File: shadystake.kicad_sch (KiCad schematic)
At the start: 15 parts, among them J1 6P6C, J2 6P6C, J3 6P6C, J4 6P6C, J5 6P6C, J6 6P6C, J7 8P8C

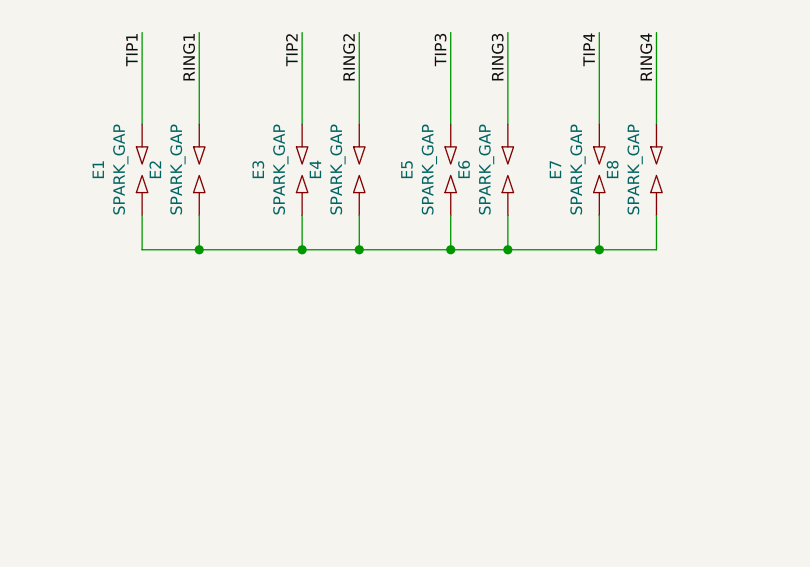
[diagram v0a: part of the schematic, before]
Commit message: really rough draft of physical layout
⚠ spark gap footprints still completely missing

modular jack footprints assumed to be the Amphenol SKU.

The Board.Cuts shape still seems like awkward proportions, but in a
manufacturable size.
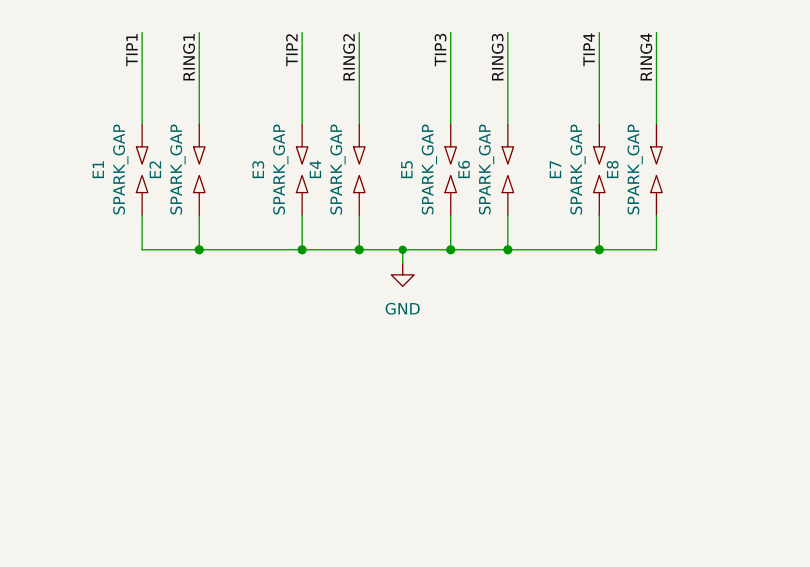
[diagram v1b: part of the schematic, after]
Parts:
- J1, J2, J3, J4, J5, J6: footprint Connect:RJ12_E -> Connector_RJ:RJ12_Amphenol_54601
- J7: footprint Connect:RJ45_8 -> Connector_RJ:RJ45_Amphenol_54602-x08_Horizontal
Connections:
- net GND: now reaches E1.1, E2.1, E3.1, E4.1, E5.1, E6.1, E7.1, E8.1

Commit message: shadystake: make it roughly the proportions of the Shadytel logo
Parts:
- E1, E2, E3, E4, E5, E6, E7, E8: footprint (none) -> Shadystake:Sparkgap_JLC
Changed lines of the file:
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@@
     (property "Reference" "E1" (id 0) (at 133.604 91.44 0))
     (property "Value" "SPARK_GAP" (id 1) (at 135.9154 91.44 0))
-    (property "Footprint" "" (id 2) (at 140.208 91.44 0)
+    (property "Footprint" "Shadystake:Sparkgap_JLC" (id 2) (at 140.208 91.44 0)
       (effects (font (size 1.27 1.27)) hide)
     )
@@
     (property "Reference" "E2" (id 0) (at 139.954 91.44 0))
     (property "Value" "SPARK_GAP" (id 1) (at 142.2654 91.44 0))
-    (property "Footprint" "" (id 2) (at 146.558 91.44 0)
+    (property "Footprint" "Shadystake:Sparkgap_JLC" (id 2) (at 146.558 91.44 0)
       (effects (font (size 1.27 1.27)) hide)
     )
@@
     (property "Reference" "E4" (id 0) (at 157.734 91.44 0))
     (property "Value" "SPARK_GAP" (id 1) (at 160.0454 91.44 0))
-    (property "Footprint" "" (id 2) (at 164.338 91.44 0)
+    (property "Footprint" "Shadystake:Sparkgap_JLC" (id 2) (at 164.338 91.44 0)
       (effects (font (size 1.27 1.27)) hide)
     )
@@
     (property "Reference" "E3" (id 0) (at 151.384 91.44 0))
     (property "Value" "SPARK_GAP" (id 1) (at 153.6954 91.44 0))
-    (property "Footprint" "" (id 2) (at 157.988 91.44 0)
+    (property "Footprint" "Shadystake:Sparkgap_JLC" (id 2) (at 157.988 91.44 0)
       (effects (font (size 1.27 1.27)) hide)
     )
@@
     (property "Reference" "E5" (id 0) (at 167.894 91.44 0))
     (property "Value" "SPARK_GAP" (id 1) (at 170.2054 91.44 0))
-    (property "Footprint" "" (id 2) (at 174.498 91.44 0)
+    (property "Footprint" "Shadystake:Sparkgap_JLC" (id 2) (at 174.498 91.44 0)
       (effects (font (size 1.27 1.27)) hide)
     )
@@
     (property "Reference" "E6" (id 0) (at 174.244 91.44 0))
     (property "Value" "SPARK_GAP" (id 1) (at 176.5554 91.44 0))
-    (property "Footprint" "" (id 2) (at 180.848 91.44 0)
+    (property "Footprint" "Shadystake:Sparkgap_JLC" (id 2) (at 180.848 91.44 0)
       (effects (font (size 1.27 1.27)) hide)
     )
@@
     (property "Reference" "E7" (id 0) (at 184.404 91.44 0))
     (property "Value" "SPARK_GAP" (id 1) (at 186.7154 91.44 0))
-    (property "Footprint" "" (id 2) (at 191.008 91.44 0)
+    (property "Footprint" "Shadystake:Sparkgap_JLC" (id 2) (at 191.008 91.44 0)
       (effects (font (size 1.27 1.27)) hide)
     )
@@
     (property "Reference" "E8" (id 0) (at 190.754 91.44 0))
     (property "Value" "SPARK_GAP" (id 1) (at 193.0654 91.44 0))
-    (property "Footprint" "" (id 2) (at 197.358 91.44 0)
+    (property "Footprint" "Shadystake:Sparkgap_JLC" (id 2) (at 197.358 91.44 0)
       (effects (font (size 1.27 1.27)) hide)
     )
@@
     )
     (path "/00000000-0000-0000-0000-00005e77f6d5"
-      (reference "E1") (unit 1) (value "SPARK_GAP") (footprint "")
+      (reference "E1") (unit 1) (value "SPARK_GAP") (footprint "Shadystake:Sparkgap_JLC")
     )
     (path "/00000000-0000-0000-0000-00005e77fd1f"
-      (reference "E2") (unit 1) (value "SPARK_GAP") (footprint "")
+      (reference "E2") (unit 1) (value "SPARK_GAP") (footprint "Shadystake:Sparkgap_JLC")
     )
     (path "/00000000-0000-0000-0000-00005e7804e5"
-      (reference "E3") (unit 1) (value "SPARK_GAP") (footprint "")
+      (reference "E3") (unit 1) (value "SPARK_GAP") (footprint "Shadystake:Sparkgap_JLC")
     )
     (path "/00000000-0000-0000-0000-00005e77fe7e"
-      (reference "E4") (unit 1) (value "SPARK_GAP") (footprint "")
+      (reference "E4") (unit 1) (value "SPARK_GAP") (footprint "Shadystake:Sparkgap_JLC")
     )
     (path "/00000000-0000-0000-0000-00005e780786"
-      (reference "E5") (unit 1) (value "SPARK_GAP") (footprint "")
+      (reference "E5") (unit 1) (value "SPARK_GAP") (footprint "Shadystake:Sparkgap_JLC")
     )
     (path "/00000000-0000-0000-0000-00005e780e1b"
-      (reference "E6") (unit 1) (value "SPARK_GAP") (footprint "")
+      (reference "E6") (unit 1) (value "SPARK_GAP") (footprint "Shadystake:Sparkgap_JLC")
     )
     (path "/00000000-0000-0000-0000-00005e7810bc"
-      (reference "E7") (unit 1) (value "SPARK_GAP") (footprint "")
+      (reference "E7") (unit 1) (value "SPARK_GAP") (footprint "Shadystake:Sparkgap_JLC")
     )
     (path "/00000000-0000-0000-0000-00005e781e02"
-      (reference "E8") (unit 1) (value "SPARK_GAP") (footprint "")
+      (reference "E8") (unit 1) (value "SPARK_GAP") (footprint "Shadystake:Sparkgap_JLC")
     )
     (path "/00000000-0000-0000-0000-00005e77093f"

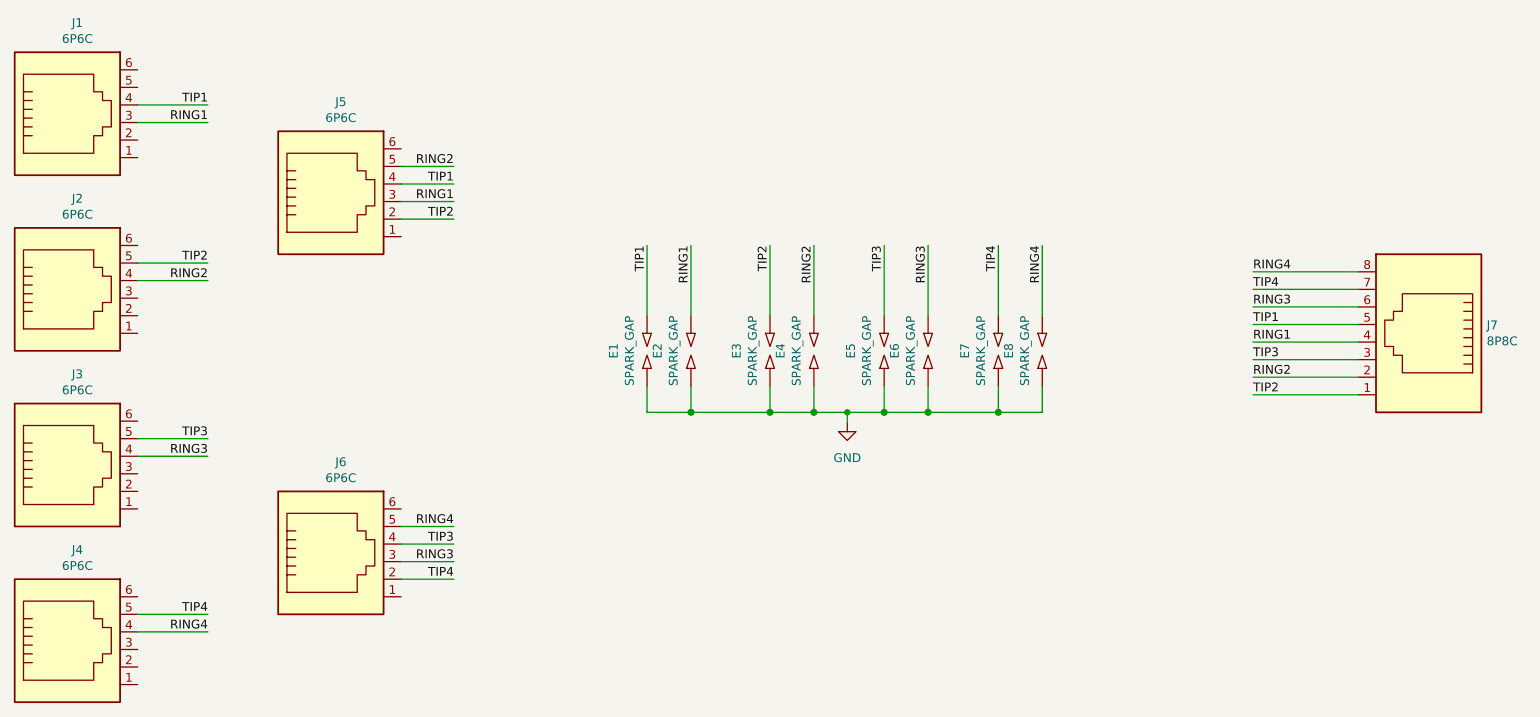
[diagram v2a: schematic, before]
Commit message: Fix pin connections on several jacks and add more spark gaps
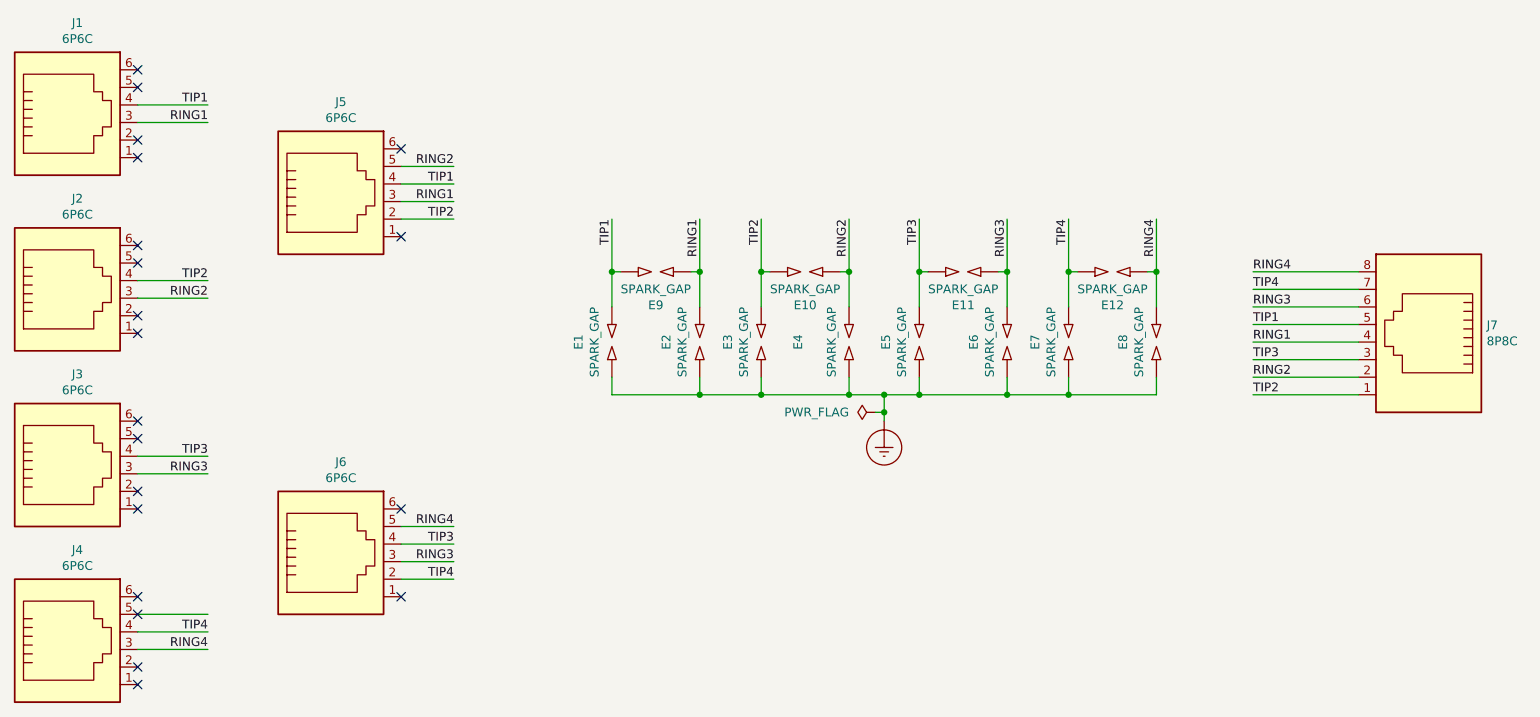
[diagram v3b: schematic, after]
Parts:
- added E10, E11, E12, E9: SPARK_GAP, shadytel:SPARKGAP, symbol shadystake-rescue:SPARK_GAP-Device
- E1, E2, E3, E4, E5, E6, E7, E8: footprint Shadystake:Sparkgap_JLC -> shadytel:SPARKGAP
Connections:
- net RING1: now also E9.1
- net RING2: now also J2.3, E10.1; no longer J2.4
- net RING3: now also J3.3, E11.1; no longer J3.4
- net RING4: now also J4.3, E12.1; no longer J4.4
- net TIP1: now also E9.2
- net TIP2: now also J2.4, E10.2; no longer J2.5
- net TIP3: now also J3.4, E11.2; no longer J3.5
- net TIP4: now also J4.4, E12.2; no longer J4.5
- net GND renamed Earth_Protective
- no-connect marks 0 -> 20
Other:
- moved on the sheet: E1, E2, E3, E4, E5, E6, E7, E8

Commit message: fix spark gaps, continuity on PCB
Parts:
- E1, E10, E11, E12, E2, E3, E4, E5, E6, E7, E8, E9: footprint shadytel:SPARKGAP -> Shadystake:Sparkgap_JLC
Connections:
- net RING2: now also E10.2; no longer E10.1
- net RING3: now also E11.2; no longer E11.1
- net TIP2: now also E10.1; no longer E10.2
- net TIP3: now also E11.1; no longer E11.2
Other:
- moved on the sheet: E10, E11
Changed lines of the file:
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@@
     (property "Reference" "E1" (id 0) (at 128.524 90.17 0))
     (property "Value" "SPARK_GAP" (id 1) (at 130.8354 90.17 0))
-    (property "Footprint" "shadytel:SPARKGAP" (id 2) (at 135.128 90.17 0)
+    (property "Footprint" "Shadystake:Sparkgap_JLC" (id 2) (at 135.128 90.17 0)
       (effects (font (size 1.27 1.27)) hide)
     )
@@
     (property "Reference" "E2" (id 0) (at 141.224 90.17 0))
     (property "Value" "SPARK_GAP" (id 1) (at 143.5354 90.17 0))
-    (property "Footprint" "shadytel:SPARKGAP" (id 2) (at 147.828 90.17 0)
+    (property "Footprint" "Shadystake:Sparkgap_JLC" (id 2) (at 147.828 90.17 0)
       (effects (font (size 1.27 1.27)) hide)
     )
@@
     (property "Reference" "E4" (id 0) (at 160.274 90.17 0))
     (property "Value" "SPARK_GAP" (id 1) (at 165.1254 90.17 0))
-    (property "Footprint" "shadytel:SPARKGAP" (id 2) (at 169.418 90.17 0)
+    (property "Footprint" "Shadystake:Sparkgap_JLC" (id 2) (at 169.418 90.17 0)
       (effects (font (size 1.27 1.27)) hide)
     )
@@
     (property "Reference" "E3" (id 0) (at 150.114 90.17 0))
     (property "Value" "SPARK_GAP" (id 1) (at 152.4254 90.17 0))
-    (property "Footprint" "shadytel:SPARKGAP" (id 2) (at 156.718 90.17 0)
+    (property "Footprint" "Shadystake:Sparkgap_JLC" (id 2) (at 156.718 90.17 0)
       (effects (font (size 1.27 1.27)) hide)
     )
@@
     (property "Reference" "E5" (id 0) (at 172.974 90.17 0))
     (property "Value" "SPARK_GAP" (id 1) (at 175.2854 90.17 0))
-    (property "Footprint" "shadytel:SPARKGAP" (id 2) (at 179.578 90.17 0)
+    (property "Footprint" "Shadystake:Sparkgap_JLC" (id 2) (at 179.578 90.17 0)
       (effects (font (size 1.27 1.27)) hide)
     )
@@
     (property "Reference" "E6" (id 0) (at 185.674 90.17 0))
     (property "Value" "SPARK_GAP" (id 1) (at 187.9854 90.17 0))
-    (property "Footprint" "shadytel:SPARKGAP" (id 2) (at 192.278 90.17 0)
+    (property "Footprint" "Shadystake:Sparkgap_JLC" (id 2) (at 192.278 90.17 0)
       (effects (font (size 1.27 1.27)) hide)
     )
@@
     (property "Reference" "E7" (id 0) (at 194.564 90.17 0))
     (property "Value" "SPARK_GAP" (id 1) (at 196.8754 90.17 0))
-    (property "Footprint" "shadytel:SPARKGAP" (id 2) (at 201.168 90.17 0)
+    (property "Footprint" "Shadystake:Sparkgap_JLC" (id 2) (at 201.168 90.17 0)
       (effects (font (size 1.27 1.27)) hide)
     )
@@
     (property "Reference" "E8" (id 0) (at 207.264 90.17 0))
     (property "Value" "SPARK_GAP" (id 1) (at 209.5754 90.17 0))
-    (property "Footprint" "shadytel:SPARKGAP" (id 2) (at 213.868 90.17 0)
+    (property "Footprint" "Shadystake:Sparkgap_JLC" (id 2) (at 213.868 90.17 0)
       (effects (font (size 1.27 1.27)) hide)
     )
@@
     (pin "2")
   )
-  (symbol (lib_id "shadystake-rescue:SPARK_GAP-Device") (at 161.29 80.01 180) (unit 1)
+  (symbol (lib_id "shadystake-rescue:SPARK_GAP-Device") (at 161.29 80.01 0) (mirror x) (unit 1)
     (in_bom yes) (on_board yes)
     (property "Reference" "E10" (id 0) (at 161.29 84.836 0))
     (property "Value" "SPARK_GAP" (id 1) (at 161.29 82.5246 0))
-    (property "Footprint" "shadytel:SPARKGAP" (id 2) (at 161.29 78.232 0)
+    (property "Footprint" "Shadystake:Sparkgap_JLC" (id 2) (at 161.29 78.232 0)
       (effects (font (size 1.27 1.27)) hide)
     )
@@
     (pin "2")
   )
-  (symbol (lib_id "shadystake-rescue:SPARK_GAP-Device") (at 184.15 80.01 180) (unit 1)
+  (symbol (lib_id "shadystake-rescue:SPARK_GAP-Device") (at 184.15 80.01 0) (mirror x) (unit 1)
     (in_bom yes) (on_board yes)
     (property "Reference" "E11" (id 0) (at 184.15 84.836 0))
     (property "Value" "SPARK_GAP" (id 1) (at 184.15 82.5246 0))
-    (property "Footprint" "shadytel:SPARKGAP" (id 2) (at 184.15 78.232 0)
+    (property "Footprint" "Shadystake:Sparkgap_JLC" (id 2) (at 184.15 78.232 0)
       (effects (font (size 1.27 1.27)) hide)
     )
@@
     (property "Reference" "E12" (id 0) (at 205.74 84.836 0))
     (property "Value" "SPARK_GAP" (id 1) (at 205.74 82.5246 0))
-    (property "Footprint" "shadytel:SPARKGAP" (id 2) (at 205.74 78.232 0)
+    (property "Footprint" "Shadystake:Sparkgap_JLC" (id 2) (at 205.74 78.232 0)
       (effects (font (size 1.27 1.27)) hide)
     )
@@
     (property "Reference" "E9" (id 0) (at 139.7 84.836 0))
     (property "Value" "SPARK_GAP" (id 1) (at 139.7 82.5246 0))
-    (property "Footprint" "shadytel:SPARKGAP" (id 2) (at 139.7 78.232 0)
+    (property "Footprint" "Shadystake:Sparkgap_JLC" (id 2) (at 139.7 78.232 0)
       (effects (font (size 1.27 1.27)) hide)
     )
@@
     )
     (path "/00000000-0000-0000-0000-00005e77f6d5"
-      (reference "E1") (unit 1) (value "SPARK_GAP") (footprint "shadytel:SPARKGAP")
+      (reference "E1") (unit 1) (value "SPARK_GAP") (footprint "Shadystake:Sparkgap_JLC")
     )
     (path "/00000000-0000-0000-0000-00005e77fd1f"
-      (reference "E2") (unit 1) (value "SPARK_GAP") (footprint "shadytel:SPARKGAP")
+      (reference "E2") (unit 1) (value "SPARK_GAP") (footprint "Shadystake:Sparkgap_JLC")
     )
     (path "/00000000-0000-0000-0000-00005e7804e5"
-      (reference "E3") (unit 1) (value "SPARK_GAP") (footprint "shadytel:SPARKGAP")
+      (reference "E3") (unit 1) (value "SPARK_GAP") (footprint "Shadystake:Sparkgap_JLC")
     )
     (path "/00000000-0000-0000-0000-00005e77fe7e"
-      (reference "E4") (unit 1) (value "SPARK_GAP") (footprint "shadytel:SPARKGAP")
+      (reference "E4") (unit 1) (value "SPARK_GAP") (footprint "Shadystake:Sparkgap_JLC")
     )
     (path "/00000000-0000-0000-0000-00005e780786"
-      (reference "E5") (unit 1) (value "SPARK_GAP") (footprint "shadytel:SPARKGAP")
+      (reference "E5") (unit 1) (value "SPARK_GAP") (footprint "Shadystake:Sparkgap_JLC")
     )
     (path "/00000000-0000-0000-0000-00005e780e1b"
-      (reference "E6") (unit 1) (value "SPARK_GAP") (footprint "shadytel:SPARKGAP")
+      (reference "E6") (unit 1) (value "SPARK_GAP") (footprint "Shadystake:Sparkgap_JLC")
     )
     (path "/00000000-0000-0000-0000-00005e7810bc"
-      (reference "E7") (unit 1) (value "SPARK_GAP") (footprint "shadytel:SPARKGAP")
+      (reference "E7") (unit 1) (value "SPARK_GAP") (footprint "Shadystake:Sparkgap_JLC")
     )
     (path "/00000000-0000-0000-0000-00005e781e02"
-      (reference "E8") (unit 1) (value "SPARK_GAP") (footprint "shadytel:SPARKGAP")
+      (reference "E8") (unit 1) (value "SPARK_GAP") (footprint "Shadystake:Sparkgap_JLC")
     )
     (path "/a099766c-5db3-4006-8bf9-84d99ea23762"
-      (reference "E9") (unit 1) (value "SPARK_GAP") (footprint "shadytel:SPARKGAP")
+      (reference "E9") (unit 1) (value "SPARK_GAP") (footprint "Shadystake:Sparkgap_JLC")
     )
     (path "/0344f435-3dd8-43ba-b18c-7b81844faf76"
-      (reference "E10") (unit 1) (value "SPARK_GAP") (footprint "shadytel:SPARKGAP")
+      (reference "E10") (unit 1) (value "SPARK_GAP") (footprint "Shadystake:Sparkgap_JLC")
     )
     (path "/0ed11af5-0934-43bf-b32a-17d5b78ef9bf"
-      (reference "E11") (unit 1) (value "SPARK_GAP") (footprint "shadytel:SPARKGAP")
+      (reference "E11") (unit 1) (value "SPARK_GAP") (footprint "Shadystake:Sparkgap_JLC")
     )
     (path "/2c110285-a58c-48e5-8202-0cf404b637f9"
-      (reference "E12") (unit 1) (value "SPARK_GAP") (footprint "shadytel:SPARKGAP")
+      (reference "E12") (unit 1) (value "SPARK_GAP") (footprint "Shadystake:Sparkgap_JLC")
     )
     (path "/00000000-0000-0000-0000-00005e77093f"

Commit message: Lay out design
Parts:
- E1, E10, E11, E12, E2, E3, E4, E5, E6, E7, E8, E9: footprint Shadystake:Sparkgap_JLC -> Shadystake:Spark_Gap_Teeth
- J1, J2, J3, J4, J5, J6: footprint Connector_RJ:RJ12_Amphenol_54601 -> Shadystake:6P4C_Vert
- J7: footprint Connector_RJ:RJ45_Amphenol_54602-x08_Horizontal -> Shadystake:8P8C_Hor
